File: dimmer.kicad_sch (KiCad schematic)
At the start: 45 parts, among them J1 Conn_01x02, J2 Conn_01x02, J3 Conn_01x06, Q1 WNM2030, Q10 HY1503C1, Q2 WNM2030, Q3 WNM2030, Q4 WNM2030, Q5 WNM2030, Q6 HY1503C1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

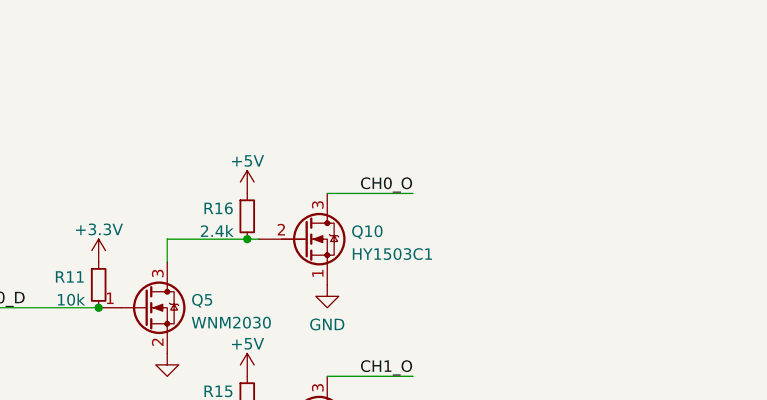
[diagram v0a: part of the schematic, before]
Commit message: Update for in-stock parts
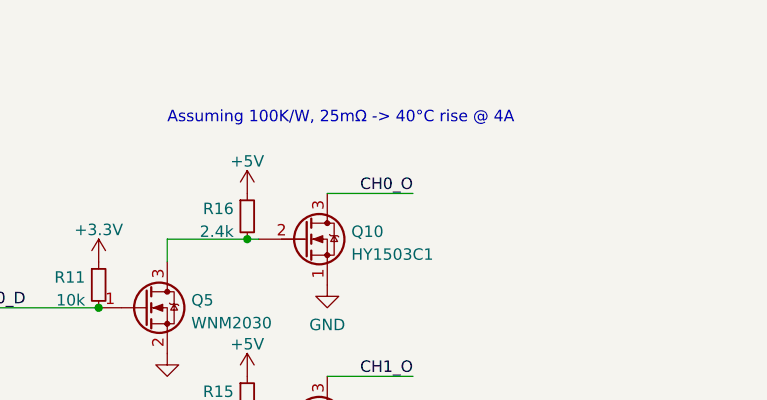
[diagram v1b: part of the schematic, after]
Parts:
- Q10, Q6, Q7, Q8, Q9: LCSC C358109 -> C315567
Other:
- note added: "Assuming 100K/W, 25mΩ -> 40°C rise @ 4A"
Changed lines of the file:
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@@
     (stroke (width 0) (type default) (color 0 0 0 0))
+  )
+  (text "Assuming 100K/W, 25mΩ -> 40°C rise @ 4A" (at 198.12 29.21 0)
+    (effects (font (size 1.27 1.27)) (justify left bottom))
   )
   (text "10k pot input\nmanual control" (at 72.39 55.245 0)
@@
       (effects (font (size 1.27 1.27)) (justify left) hide)
     )
-    (property "LCSC" "C358109" (id 5) (at 213.36 62.23 0)
+    (property "LCSC" "C315567" (id 5) (at 213.36 62.23 0)
+      (effects (font (size 1.27 1.27)) hide)
+    )
+    (property "Description" "Rds_on < 25mΩ @ Vgs=5V" (id 6) (at 213.36 62.23 0)
       (effects (font (size 1.27 1.27)) hide)
     )
@@
       (effects (font (size 1.27 1.27)) (justify left) hide)
     )
-    (property "LCSC" "C358109" (id 5) (at 213.36 125.73 0)
+    (property "LCSC" "C315567" (id 5) (at 213.36 125.73 0)
+      (effects (font (size 1.27 1.27)) hide)
+    )
+    (property "Description" "Rds_on < 25mΩ @ Vgs=5V" (id 6) (at 213.36 125.73 0)
       (effects (font (size 1.27 1.27)) hide)
     )
@@
       (effects (font (size 1.27 1.27)) (justify left) hide)
     )
-    (property "LCSC" "C358109" (id 5) (at 213.36 104.14 0)
+    (property "LCSC" "C315567" (id 5) (at 213.36 104.14 0)
+      (effects (font (size 1.27 1.27)) hide)
+    )
+    (property "Description" "Rds_on < 25mΩ @ Vgs=5V" (id 6) (at 213.36 104.14 0)
       (effects (font (size 1.27 1.27)) hide)
     )
@@
       (effects (font (size 1.27 1.27)) (justify left) hide)
     )
-    (property "LCSC" "C358109" (id 5) (at 213.36 41.91 0)
+    (property "LCSC" "C315567" (id 5) (at 213.36 41.91 0)
+      (effects (font (size 1.27 1.27)) hide)
+    )
+    (property "Description" "Rds_on < 25mΩ @ Vgs=5V" (id 5) (at 213.36 41.91 0)
       (effects (font (size 1.27 1.27)) hide)
     )
@@
       (effects (font (size 1.27 1.27)) (justify left) hide)
     )
-    (property "LCSC" "C358109" (id 5) (at 213.36 82.55 0)
-      (effects (font (size 1.27 1.27)) hide)
-    )
+    (property "LCSC" "C315567" (id 5) (at 213.36 82.55 0)
+      (effects (font (size 1.27 1.27)) hide)
+    )
+    (property "Description" "Rds_on < 25mΩ @ Vgs=5V" (id 6) (at 213.36 82.55 0)
+      (effects (font (size 1.27 1.27)) hide)
+    )

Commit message: Disconnect CH0 from on-board LED
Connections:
- net CH0_D: now also U1.19 (GPIO4); no longer U1.17 (GPIO2)
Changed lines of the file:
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@@
   )
   (no_connect (at 146.685 66.04))
-  (no_connect (at 146.685 63.5))
+  (no_connect (at 146.685 58.42))
   (no_connect (at 116.205 78.74))
   (no_connect (at 116.205 81.28))
@@
     (stroke (width 0) (type default) (color 0 0 0 0))
   )
-  (wire (pts (xy 146.685 58.42) (xy 153.67 58.42))
+  (wire (pts (xy 146.685 63.5) (xy 153.67 63.5))
     (stroke (width 0) (type default) (color 0 0 0 0))
   )
@@
     (effects (font (size 1.27 1.27)) (justify right bottom))
   )
-  (label "CH0_D" (at 153.67 58.42 180)
+  (label "CH0_D" (at 153.67 63.5 180)
     (effects (font (size 1.27 1.27)) (justify right bottom))
   )
@@
       (effects (font (size 1.27 1.27)) hide)
     )
-    (property "Description" "Rds_on < 25mΩ @ Vgs=5V" (id 5) (at 213.36 41.91 0)
-      (effects (font (size 1.27 1.27)) hide)
-    )
+    (property "Description" "Rds_on < 25mΩ @ Vgs=5V" (id 6) (at 213.36 41.91 0)
+      (effects (font (size 1.27 1.27)) hide)
+    )

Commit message: Increase 3.3V regulator pad size
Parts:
- J2: footprint Connector_Wire:SolderWire-1sqmm_1x02_P5.4mm_D1.4mm_OD2.7mm -> Connector_Wire:SolderWire-0.75sqmm_1x02_P4.8mm_D1.25mm_OD2.3mm
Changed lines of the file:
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@@
       (effects (font (size 1.27 1.27)) hide)
     )
-    (property "Footprint" "Connector_Wire:SolderWire-1sqmm_1x02_P5.4mm_D1.4mm_OD2.7mm" (id 2) (at 20.955 22.225 0)
+    (property "Footprint" "Connector_Wire:SolderWire-0.75sqmm_1x02_P4.8mm_D1.25mm_OD2.3mm" (id 2) (at 20.955 22.225 0)
       (effects (font (size 1.27 1.27)) hide)
     )
@@
     )
     (path "/a394cec0-9537-42e9-9d58-c1a5f15b790c"
-      (reference "J2") (unit 1) (value "Conn_01x02") (footprint "Connector_Wire:SolderWire-1sqmm_1x02_P5.4mm_D1.4mm_OD2.7mm")
+      (reference "J2") (unit 1) (value "Conn_01x02") (footprint "Connector_Wire:SolderWire-0.75sqmm_1x02_P4.8mm_D1.25mm_OD2.3mm")
     )
     (path "/c1d11b83-3322-46f4-a04c-3eb40838b09a"

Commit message: Add tooling holes
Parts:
- added H1, H2: MountingHole, Library:ToolingHole, symbol Mechanical:MountingHole
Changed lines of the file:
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@@
     (effects (font (size 1.27 1.27)) (justify left bottom))
+  )
+  (symbol (lib_id "Mechanical:MountingHole") (at 33.655 184.785 0) (unit 1)
+    (in_bom no) (on_board yes) (fields_autoplaced)
+    (property "Reference" "H2" (id 0) (at 36.195 183.9503 0)
+      (effects (font (size 1.27 1.27)) (justify left))
+    )
+    (property "Value" "MountingHole" (id 1) (at 36.195 186.4872 0)
+      (effects (font (size 1.27 1.27)) (justify left))
+    )
+    (property "Footprint" "Library:ToolingHole" (id 2) (at 33.655 184.785 0)
+      (effects (font (size 1.27 1.27)) hide)
+    )
+    (property "Datasheet" "~" (id 3) (at 33.655 184.785 0)
+      (effects (font (size 1.27 1.27)) hide)
+    )
   )
   (symbol (lib_id "Device:Q_NMOS_GSD") (at 195.58 49.53 0) (unit 1)
@@
     (pin "1")
     (pin "2")
+  )
+  (symbol (lib_id "Mechanical:MountingHole") (at 33.655 179.07 0) (unit 1)
+    (in_bom no) (on_board yes) (fields_autoplaced)
+    (property "Reference" "H1" (id 0) (at 36.195 178.2353 0)
+      (effects (font (size 1.27 1.27)) (justify left))
+    )
+    (property "Value" "MountingHole" (id 1) (at 36.195 180.7722 0)
+      (effects (font (size 1.27 1.27)) (justify left))
+    )
+    (property "Footprint" "Library:ToolingHole" (id 2) (at 33.655 179.07 0)
+      (effects (font (size 1.27 1.27)) hide)
+    )
+    (property "Datasheet" "~" (id 3) (at 33.655 179.07 0)
+      (effects (font (size 1.27 1.27)) hide)
+    )
   )
   (symbol (lib_id "Graphic:Logo_Open_Hardware_Small") (at 121.92 179.07 0) (unit 1)
@@
       (reference "C10") (unit 1) (value "10u 50V") (footprint "Capacitor_SMD:C_0805_2012Metric")
     )
+    (path "/0debaeb9-ae7b-4fd1-82b0-449f14ebe0f9"
+      (reference "H1") (unit 1) (value "MountingHole") (footprint "Library:ToolingHole")
+    )
+    (path "/0087697f-d903-407f-a3cd-2425ea9b370b"
+      (reference "H2") (unit 1) (value "MountingHole") (footprint "Library:ToolingHole")
+    )
     (path "/4a144960-67e8-439d-82be-95406fe8c5b5"
